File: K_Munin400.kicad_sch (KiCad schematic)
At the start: 93 parts, among them IC2 ACHS-7123-000E, J1 Conn_Coaxial, J19 To P.A., J2 Conn_Coaxial, J3 Conn_02x03_Odd_Even, J5 Wurth Redcube 7461057, J6 Phoenix/1711725, J7 Wurth Redcube 7461057, Q1 MRF300AN tab dwn, Q2 MRF300BN tab up, Q4 BSS84, T1 BN43-202 3:1, T2 FT-114A-61, T3 FT-114A-61, T4 FT-114A-61, U1 LM358, U2 LM78M05_TO252, U3 LMC660AIM_NOPB

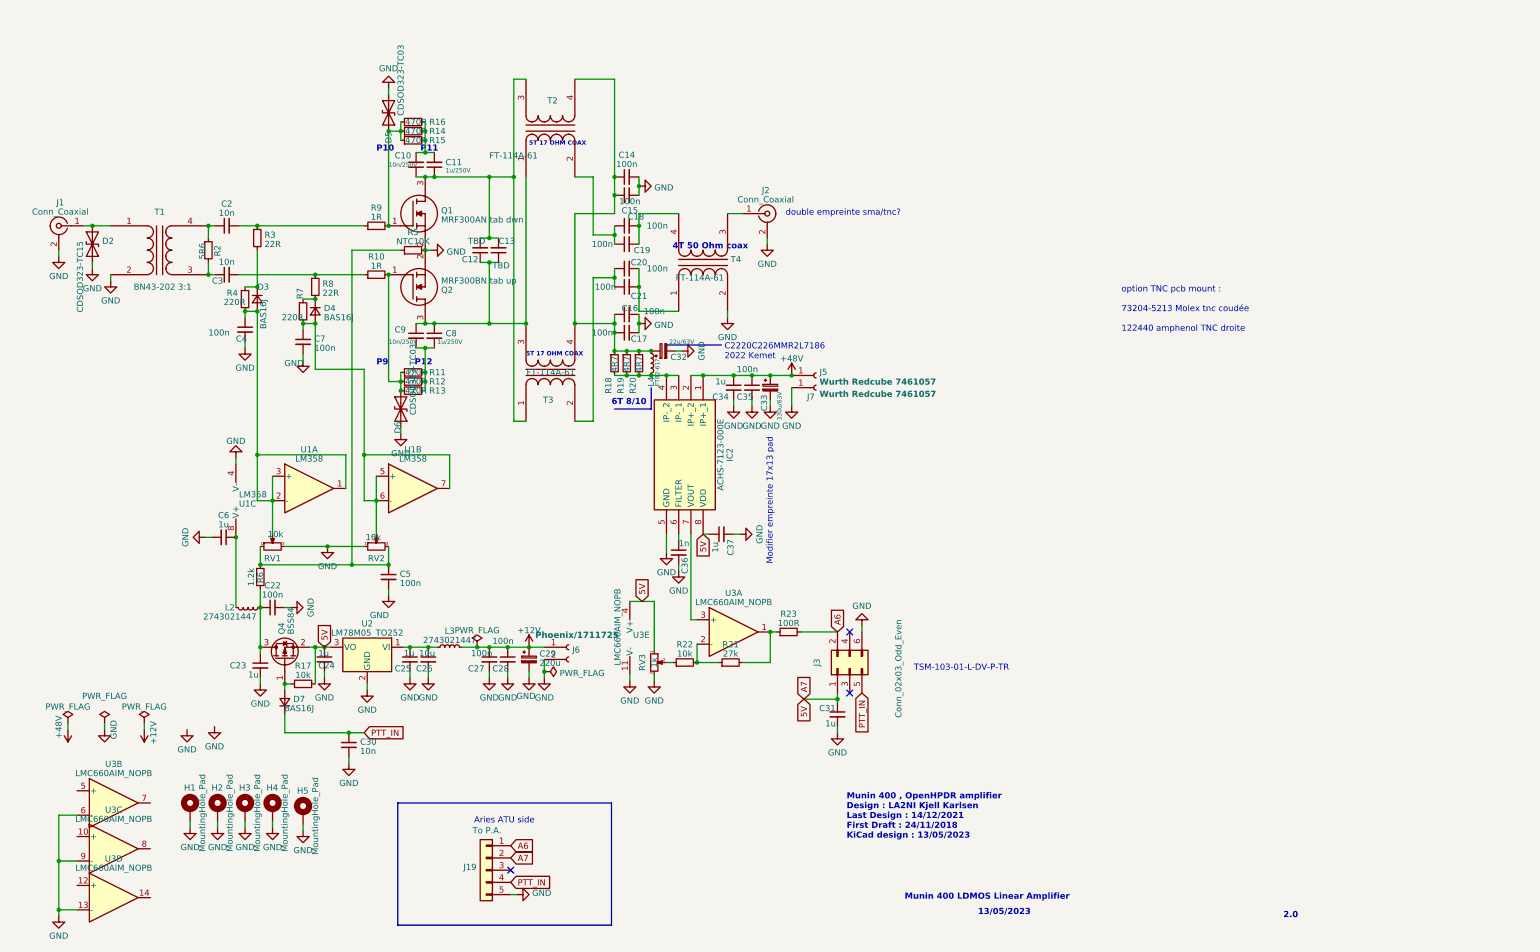
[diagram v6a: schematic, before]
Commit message: kicad 10 update, minor schematic changes
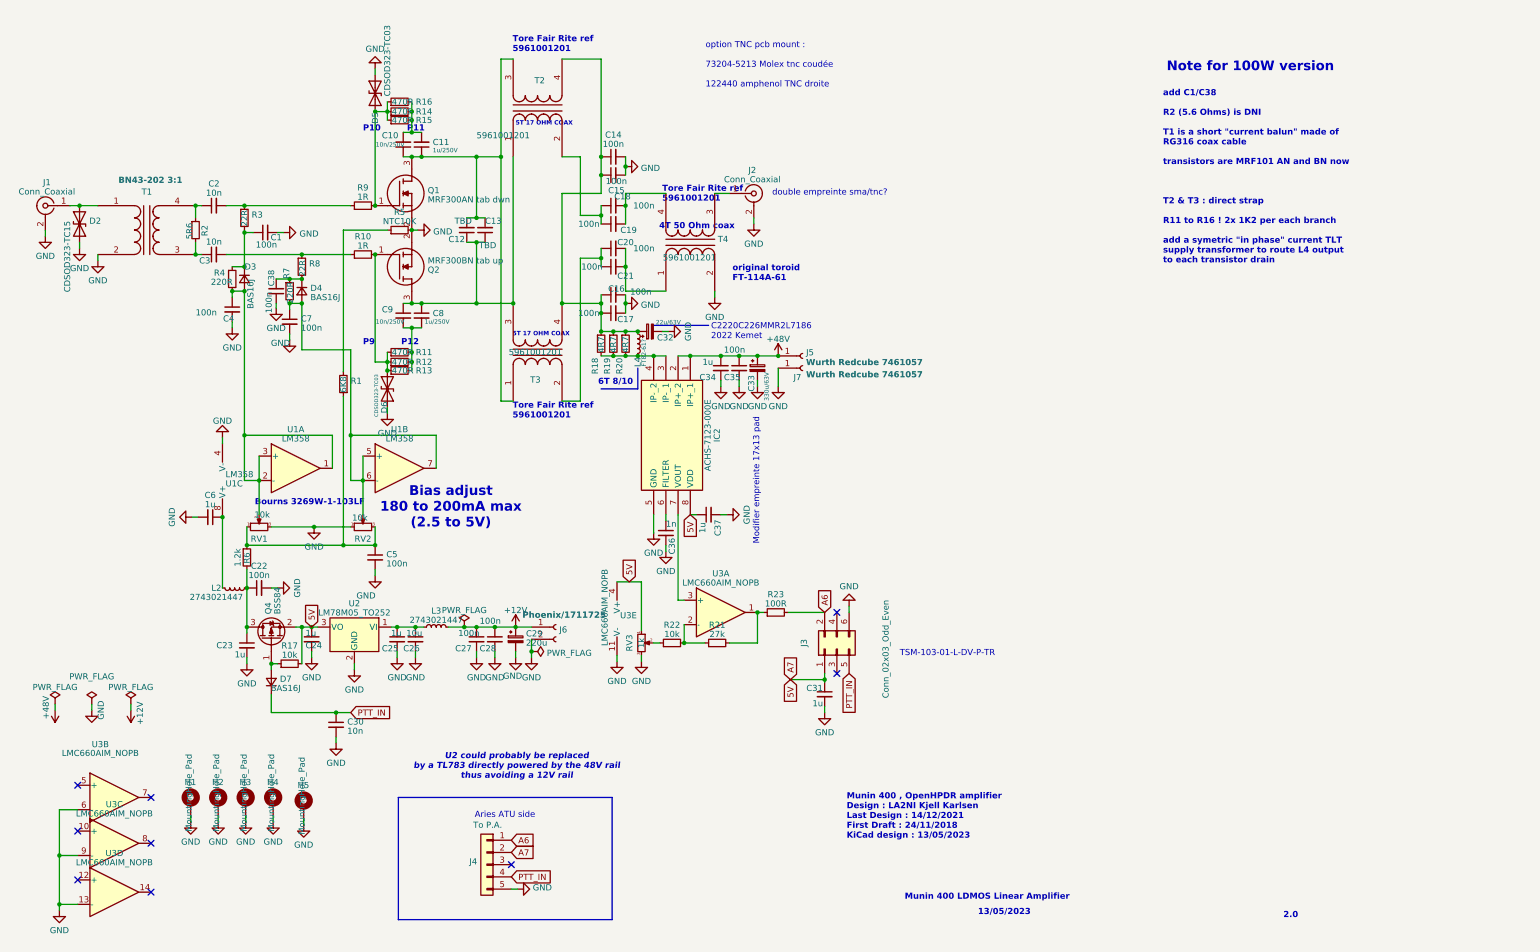
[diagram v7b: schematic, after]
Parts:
- added C1, C38: 100n, Capacitor_SMD:C_0805_2012Metric, symbol Device:C_Small
- added R1: 6K8, Resistor_SMD:R_0805_2012Metric_Pad1.20x1.40mm_HandSolder, symbol Device:R_Small
- J3: footprint Connector_PinHeader_2.54mm:PinHeader_2x03_P2.54mm_Vertical_SMD -> Connector_IDC:IDC-Header_2x03_P2.54mm_Vertical_SMD
- T2, T3, T4: value FT-114A-61 -> 5961001201
- renumbered J19 to J4
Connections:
- net GND: now also C1.2, C38.1
- net at D4.1 (K), R7.1, R8.2: now also C38.2
- net at C5.1, R6.1, RV1.1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: now also R1.1; no longer R5.1
- net at D3.1 (K), R3.2, R4.1: now also C1.1
- new net: R1.2, R5.1
- no-connect marks 3 -> 9
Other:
- note added: "Bias adjust 180 to 200mA max (2.5 to 5V)"
- note added: "Bourns 3269W-1-103LF"
- note added: "Note for 100W version"
- note added: "Tore Fair Rite ref 5961001201"
- note added: "U2 could probably be replaced by a TL783 directly powered by the 48V rail thus avoiding a 12V rail"
- note added: "add C1/C38 R2 (5.6 Ohms) is DNI T1 is a short "current balun" made of RG316 coax cable transistors are MRF101 AN and BN now T2 & T3 : direct strap R11 to R16 ! 2x 1K2 per each branch add a symetric "in phase" current TLT supply transformer to route L4 output to each transistor drain"
- note added: "original toroid FT-114A-61"
- moved on the sheet: C10, C11, C12, C13, C14, C15, C16, C17, C18, C19, C2, C20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
